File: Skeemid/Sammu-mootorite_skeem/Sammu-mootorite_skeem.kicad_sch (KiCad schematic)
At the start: 19 parts, among them SW1 SW_Push_Open, SW2 SW_DPST_x2, SW3 SW_Push_Open, SW4 SW_DPST_x2

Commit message: skeem
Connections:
- net D9: now reaches U7.1 (Signal)
- net D9: now also A1.24 (D9)
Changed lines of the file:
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@@
 	(title_block
 		(title "Etteande skeem")
-		(date "2025-06-20")
+		(date "2025-07-22")
 		(rev "1.0")
 		(company "Tauno Erik")
@@
 	(wire
 		(pts
+			(xy 21.59 110.49) (xy 33.02 110.49)
+		)
+		(stroke
+			(width 0)
+			(type default)
+		)
+	)
+	(wire
+		(pts
 			(xy 114.3 116.84) (xy 143.51 116.84)
 		)
@@
 		(pts
 			(xy 240.03 49.53) (xy 232.41 49.53)
+		)
+		(stroke
+			(width 0)
+			(type default)
+		)
+	)
+	(wire
+		(pts
+			(xy 187.96 97.79) (xy 195.58 97.79)
 		)
 		(stroke
@@
 		)
 	)
+	(label "D9"
+		(at 187.96 97.79 0)
+		(effects
+			(font
+				(size 1.27 1.27)
+			)
+			(justify left bottom)
+		)
+	)
 	(label "Toiteplokk_+24V"
 		(at 142.24 54.61 0)
@@
 		(effects
 			(font
+				(size 1.27 1.27)
+			)
+			(justify left bottom)
+		)
+	)
+	(label "D9"
+		(at 21.59 110.49 0)
+		(effects
+			(font

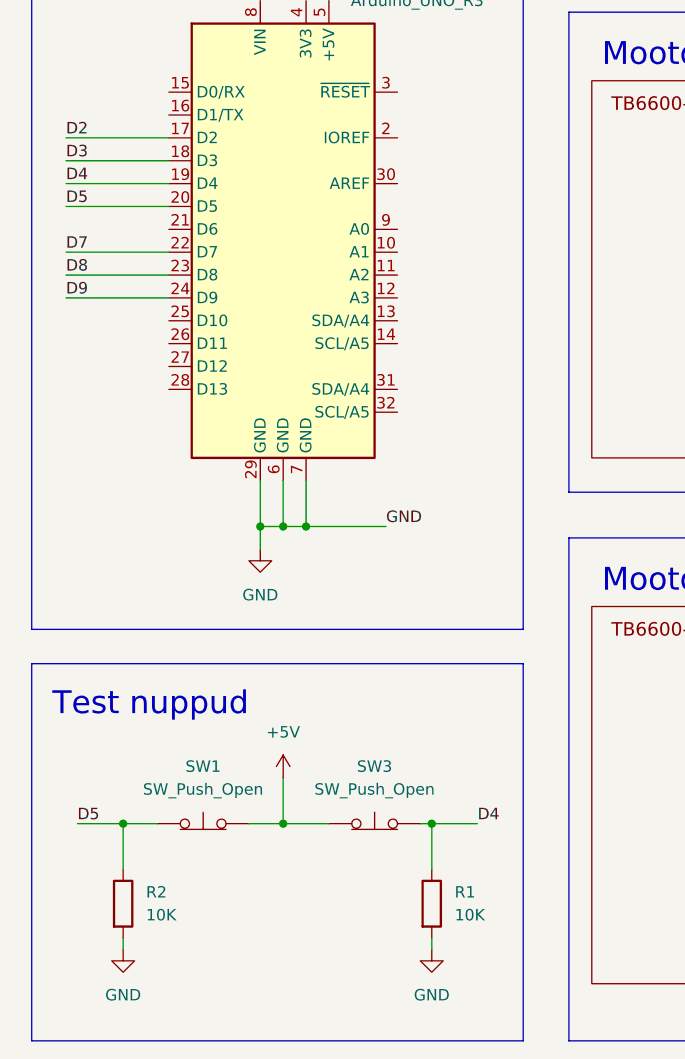
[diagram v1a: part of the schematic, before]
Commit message: Remove test button circuit from stepper motor schematic
Deleted the test button section, associated components, and wiring from the Sammu-mootorite_skeem.kicad_sch schematic. Updated schematic date and made corresponding changes to the PDF. Also added a new backup ZIP of the schematic.
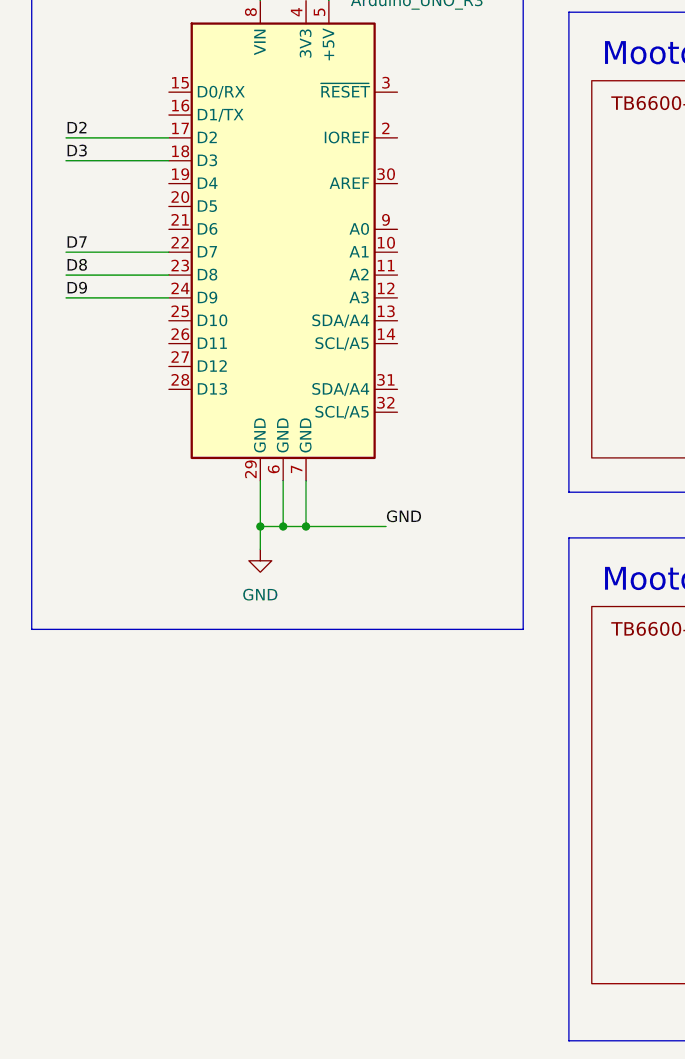
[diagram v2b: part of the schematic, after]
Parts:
- removed R1, R2: 10K, symbol Device:R
- removed SW1, SW3: SW_Push_Open, symbol Switch:SW_Push_Open
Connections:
- net D4: no longer names the net of A1.19 (D4)
- net D5: no longer names the net of A1.20 (D5)
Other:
- note removed: "Test nuppud"

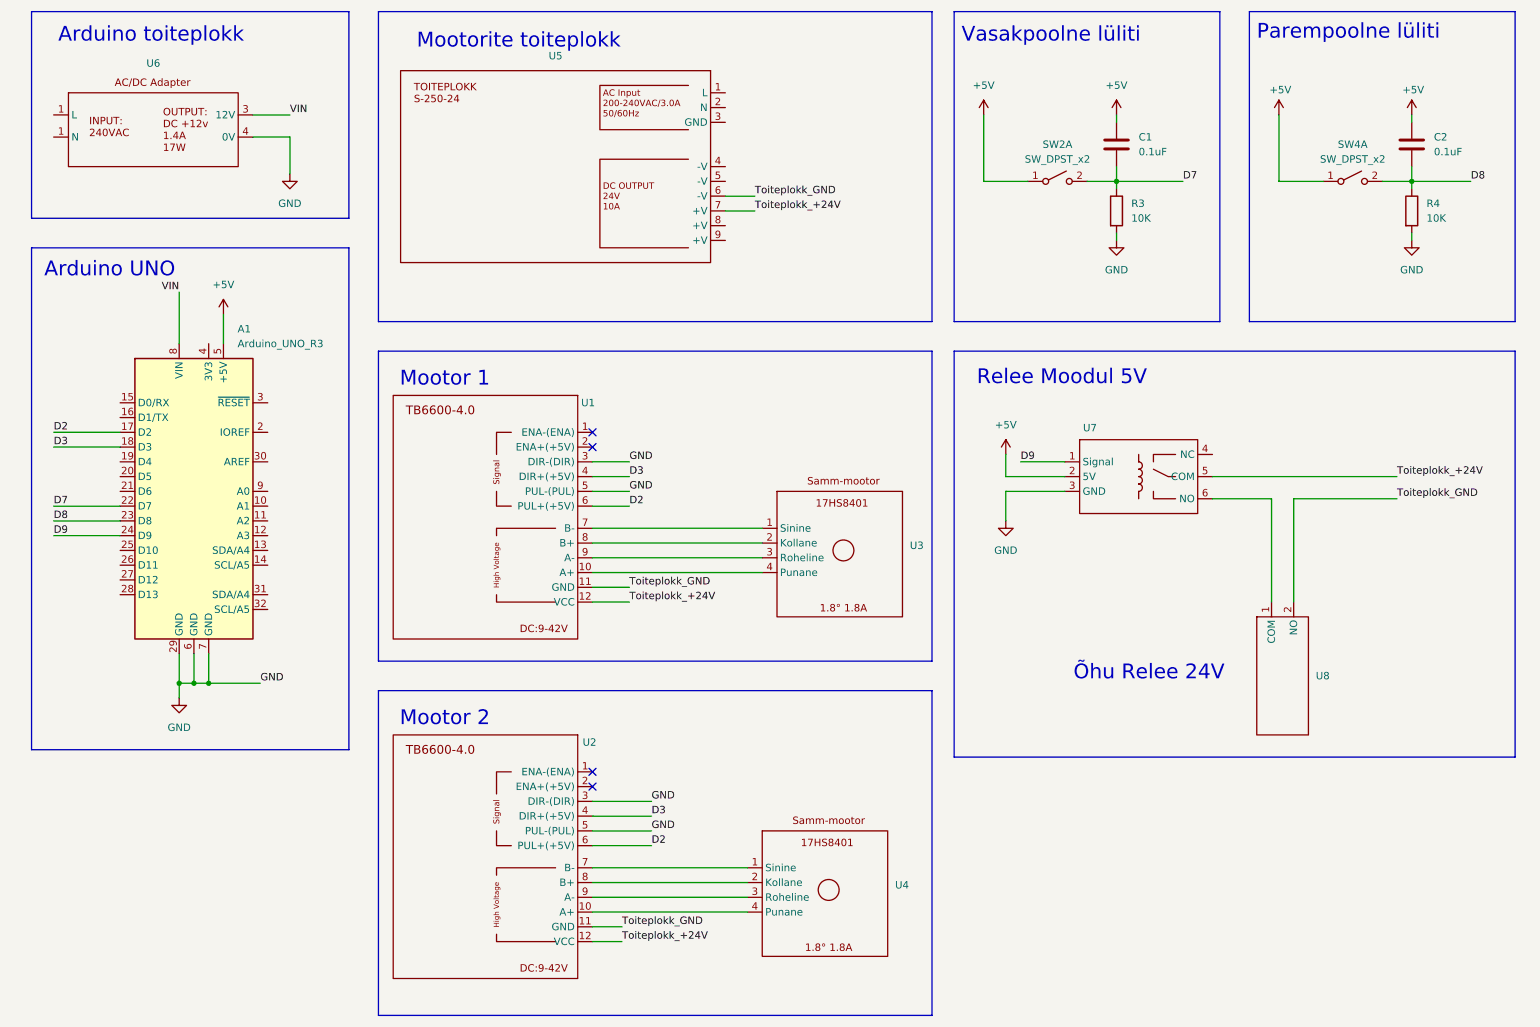
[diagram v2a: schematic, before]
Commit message: Add robot query pin and refactor push relay logic
Introduced ROBOT_PIN (D10) and related functions for querying the robot in main.cpp. Refactored relay control to use push_relee naming and adjusted timings. Updated KiCad schematic to include robot query section, new labels, and push relay module. Added schematic backup files.
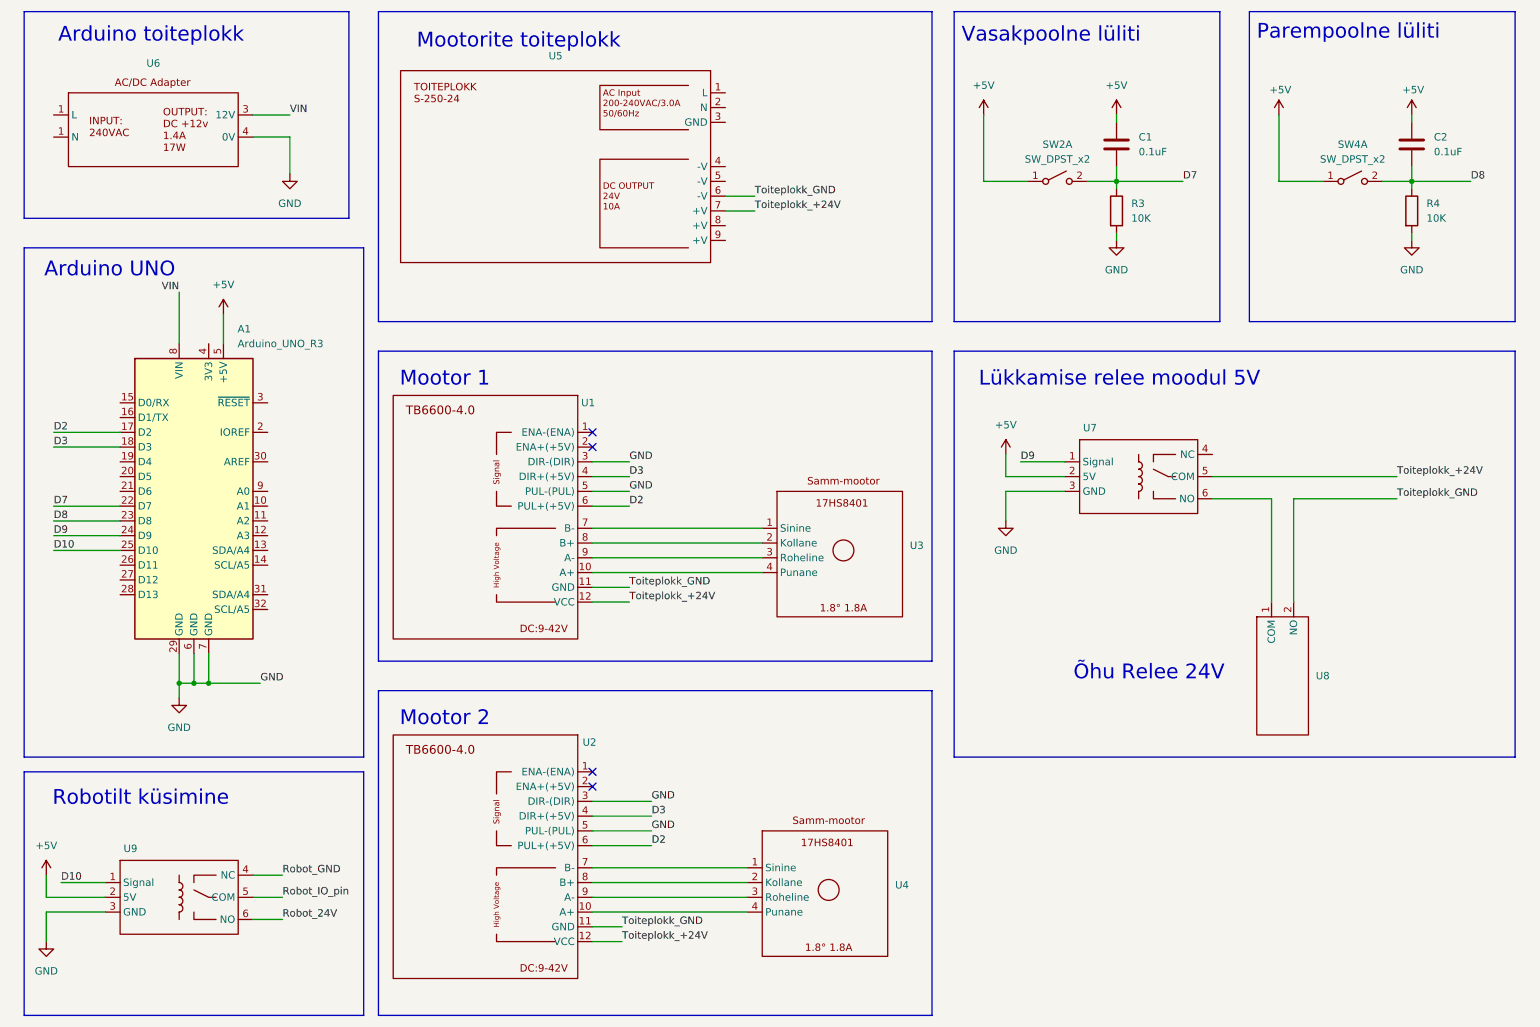
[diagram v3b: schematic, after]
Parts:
- added U9: ~, symbol Tauno_Library:Relee_Moodul
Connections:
- net +5V: now also U9.2 (5V)
- net GND: now also U9.3 (GND)
- net D10: now reaches A1.25 (D10)
- net D10: now also U9.1 (Signal)
- new net Robot_24V: U9.6 (NO)
- new net Robot_GND: U9.4 (NC)
- new net Robot_IO_pin: U9.5 (COM)
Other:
- note added: "Lükkamise relee moodul 5V"
- note added: "Robotilt küsimine"
- note removed: "Relee Moodul 5V"
